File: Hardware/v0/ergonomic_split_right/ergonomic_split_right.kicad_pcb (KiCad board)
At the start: 2 copper layers, 183 x 172.8 mm, 66 parts, among them J2 Left_Interface, SW1 R50, SW10 R31, SW11 R45, SW12 R51, SW13 R02, SW14 R12, SW15 R22, SW16 R32, SW17 R42, SW18 R54, SW19 R03, SW2 R06, SW20 R13, SW21 R23, SW22 R33, SW23 R43, SW24 R53, SW25 R04, SW26 R14, SW27 R24, SW28 R34, SW29 R44, SW3 R16, SW30 R46, SW31 R05, SW32 R15, SW33 R25, SW34 R35, SW35 R55, SW36 R10, SW37 R30, SW39 R00, SW4 R26, SW40 R_Encoder, SW5 R36, SW6 R52, SW7 R01, SW8 R11, SW9 R21, U2 PCAL9555AHF, U9 TCR2EF33

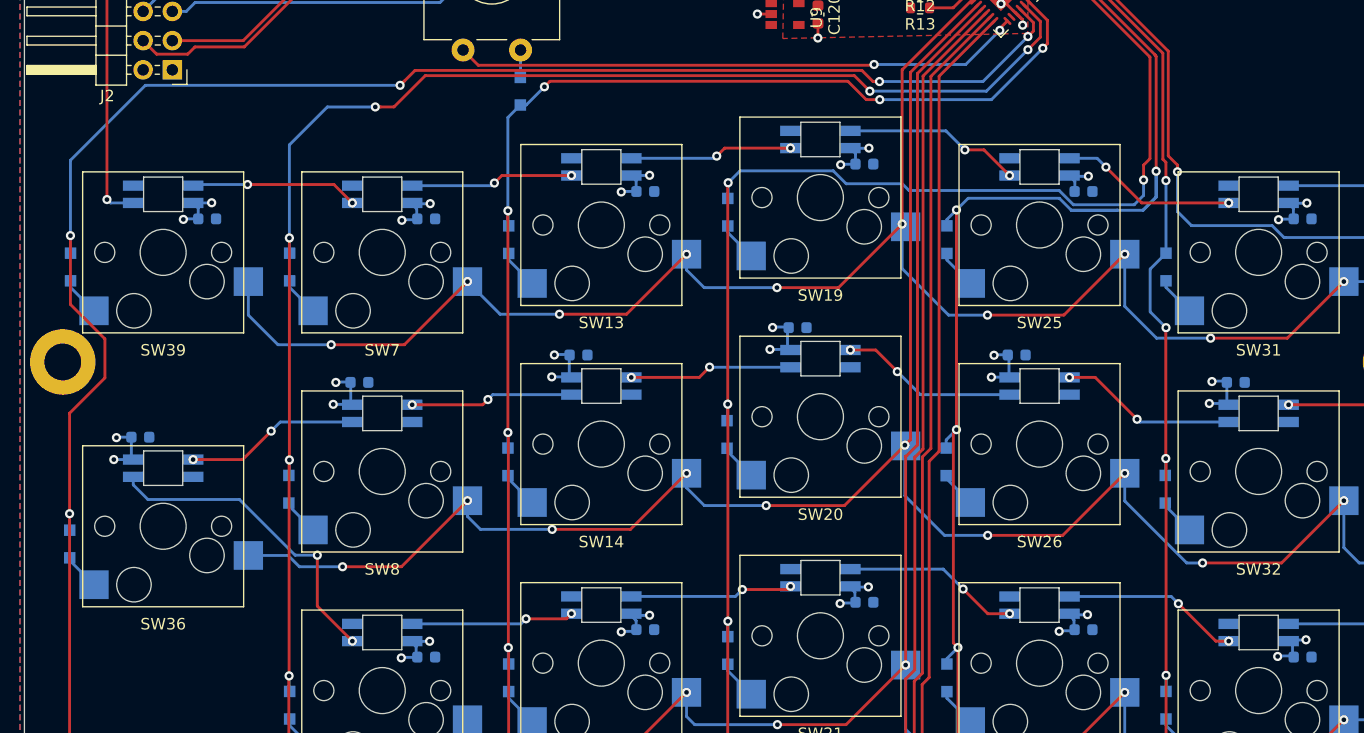
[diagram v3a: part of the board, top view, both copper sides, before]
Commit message: Adding input caps on 5V0
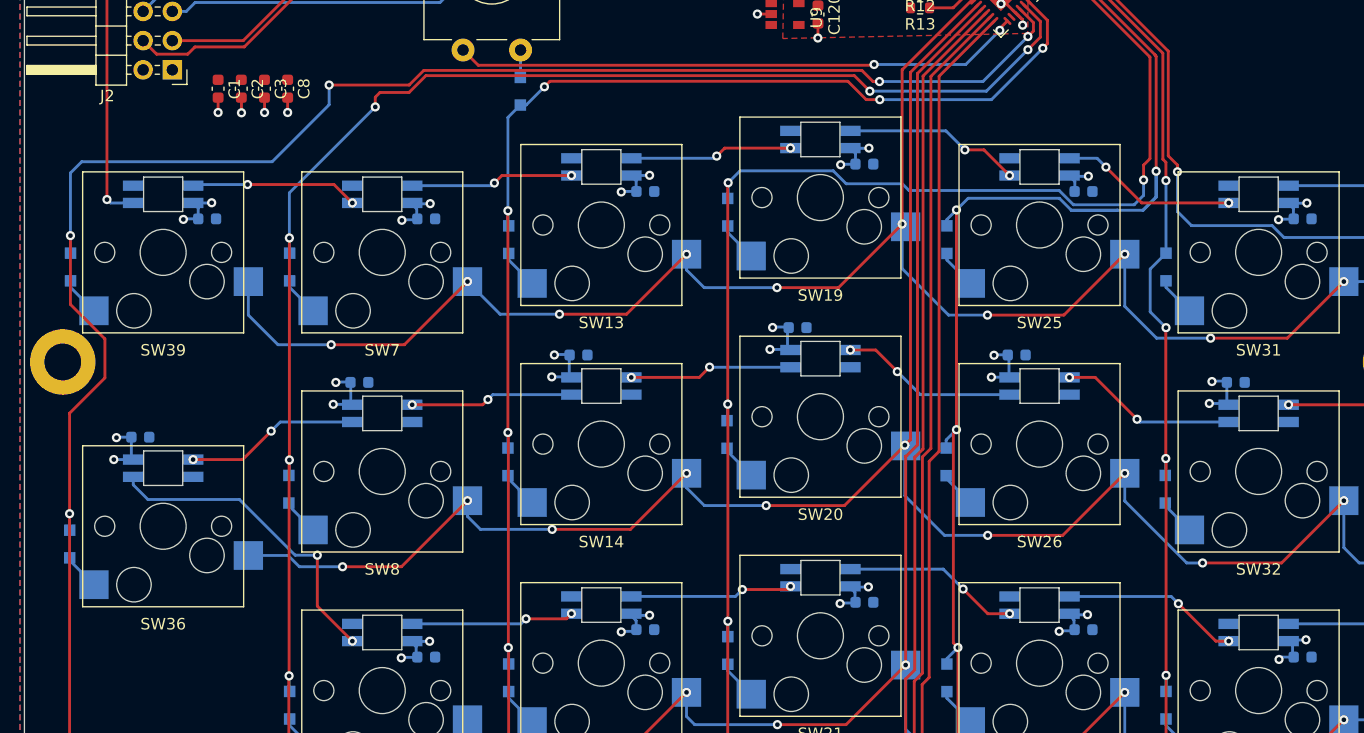
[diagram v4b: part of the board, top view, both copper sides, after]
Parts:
- added C1: 10uF, Capacitor_smd:C_0603_1608Metric, F.Cu at (157.2, 58.8)
- added C2: 1uF, Capacitor_smd:C_0603_1608Metric, F.Cu at (159.2, 58.8)
- added C3: 100nF, Capacitor_smd:C_0603_1608Metric, F.Cu at (161.2, 58.8)
- added C8: 100nF, Capacitor_smd:C_0603_1608Metric, F.Cu at (163.2, 58.8)
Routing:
- net GND: track 22.3 -> 27.4 mm, vias 12 -> 16
- net /IO Expander/COL[1]: track 199.9 -> 197.9 mm

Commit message: Cleaning up silk
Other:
- board text added: "ergonomic split - v0 Alex Binos 2022"
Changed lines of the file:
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@@
   (general
     (thickness 1.6)
-    (drawings 27)
+    (drawings 29)
     (tracks 1280)
     (zones 0)
@@
     (38 B.Mask user)
     (39 F.Mask user)
-    (40 Dwgs.User user)
-    (41 Cmts.User user)
+    (40 Dwgs.User user hide)
+    (41 Cmts.User user hide)
     (42 Eco1.User user)
     (43 Eco2.User user hide)
     (44 Edge.Cuts user)
     (45 Margin user)
-    (46 B.CrtYd user)
-    (47 F.CrtYd user)
-    (48 B.Fab user)
-    (49 F.Fab user)
+    (46 B.CrtYd user hide)
+    (47 F.CrtYd user hide)
+    (48 B.Fab user hide)
+    (49 F.Fab user hide)
   )
   (setup
@@
     (tags capacitor)
     (attr smd)
-    (fp_text reference C8 (at 0 -1.43 90) (layer F.SilkS)
+    (fp_text reference C8 (at -2.54254 -0.1143 90) (layer F.SilkS)
       (effects (font (size 1 1) (thickness 0.15)))
     )
@@
     (tags capacitor)
     (attr smd)
-    (fp_text reference C3 (at 0 -1.43 90) (layer F.SilkS)
+    (fp_text reference C3 (at -2.54254 -0.046568 90) (layer F.SilkS)
       (effects (font (size 1 1) (thickness 0.15)))
     )
@@
     (tags capacitor)
     (attr smd)
-    (fp_text reference C2 (at 0 -1.43 90) (layer F.SilkS)
+    (fp_text reference C2 (at -2.54254 -0.080434 90) (layer F.SilkS)
       (effects (font (size 1 1) (thickness 0.15)))
     )
@@
     (tags capacitor)
     (attr smd)
-    (fp_text reference C1 (at 0 -1.43 90) (layer F.SilkS)
+    (fp_text reference C1 (at -2.54254 -0.0508 90) (layer F.SilkS)
       (effects (font (size 1 1) (thickness 0.15)))
     )
@@
     (tags capacitor)
     (attr smd)
-    (fp_text reference C5 (at 0 -1.43) (layer F.SilkS)
+    (fp_text reference C5 (at -2.60096 0.06096) (layer F.SilkS)
       (effects (font (size 1 1) (thickness 0.15)))
     )
@@
     (tags capacitor)
     (attr smd)
-    (fp_text reference C7 (at 0 -1.43) (layer F.SilkS)
+    (fp_text reference C7 (at 0.06828 1.34112) (layer F.SilkS)
       (effects (font (size 1 1) (thickness 0.15)))
     )
@@
     (tags resistor)
     (attr smd)
-    (fp_text reference R12 (at 0 -1.43) (layer F.SilkS)
+    (fp_text reference R12 (at 2.24536 1.38176) (layer F.SilkS)
       (effects (font (size 1 1) (thickness 0.15)))
     )
@@
     (tags resistor)
     (attr smd)
-    (fp_text reference R13 (at 0 -1.43) (layer F.SilkS)
+    (fp_text reference R13 (at 0.091741 -1.433349) (layer F.SilkS)
       (effects (font (size 1 1) (thickness 0.15)))
     )
@@
     (descr "Alps rotary encoder, EC12E... with switch, vertical shaft, http://www.alps.com/prod/info/E/HTML/Encoder/Incremental/EC11/EC11E15204A3.html")
     (tags "rotary encoder")
-    (fp_text reference SW40 (at 2.8 -4.7 90) (layer F.SilkS)
+    (fp_text reference SW40 (at 3.78206 -5.7023 180) (layer F.SilkS)
       (effects (font (size 1 1) (thickness 0.15)))
     )
@@
     (at 225.237431 50.565538 45)
     (attr smd)
-    (fp_text reference U2 (at 0 -4.2 45) (layer F.SilkS)
+    (fp_text reference U2 (at -2.572775 -3.59901 45) (layer F.SilkS)
       (effects (font (size 1 1) (thickness 0.15)))
     )
@@
   (module custom_footprint_library:TCR2EF33_SOT25 (layer F.Cu)
     (at 205.26756 51.34864 270)
-    (fp_text reference U9 (at 1.24968 -3.937 90) (layer F.SilkS)
+    (fp_text reference U9 (at 3.43916 -1.35636 180) (layer F.SilkS)
       (effects (font (size 1 1) (thickness 0.15)))
     )
@@
       (net 5 +3V3))
   )
+  (gr_text "ergonomic split - v0\nAlex Binos 2022" (at 260.7945 52.2605) (layer F.SilkS)
+    (effects (font (size 1 1) (thickness 0.15)))
+  )
+  (gr_circle (center 222.0976 50.61712) (end 222.176626 50.61712) (layer F.SilkS) (width 0.15))
   (gr_line (start 140.335 129.8194) (end 140.333388 41.022612) (layer Edge.Cuts) (width 0.05))
   (gr_line (start 106.2482 165.2016) (end 139.398629 132.079999) (layer Edge.Cuts) (width 0.05))

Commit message: Tidying last few traces
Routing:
- net /IO Expander/ROW[5]: track 257.9 -> 256.1 mm
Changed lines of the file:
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@@
     (thickness 1.6)
     (drawings 29)
-    (tracks 1280)
+    (tracks 1277)
     (zones 0)
     (modules 70)
@@
       (outputformat 1)
       (mirror false)
-      (drillshape 1)
+      (drillshape 0)
       (scaleselection 1)
-      (outputdirectory ""))
+      (outputdirectory "gerber/"))
   )
   (net 0 "")
@@
   (segment (start 263.3345 71.7296) (end 263.3345 73.18502) (width 0.25) (layer B.Cu) (net 7))
   (via (at 240.5888 66.0146) (size 0.8) (drill 0.4) (layers F.Cu B.Cu) (net 7))
-  (segment (start 240.5888 66.0146) (end 240.5888 65.4304) (width 0.25) (layer F.Cu) (net 7))
-  (segment (start 240.5888 65.4304) (end 239.7887 64.6303) (width 0.25) (layer F.Cu) (net 7))
-  (segment (start 232.070892 47.809132) (end 239.7887 55.52694) (width 0.25) (layer F.Cu) (net 7))
-  (segment (start 227.710984 47.80913) (end 232.070892 47.809132) (width 0.25) (layer F.Cu) (net 7))
-  (segment (start 226.580922 48.939192) (end 227.710984 47.80913) (width 0.25) (layer F.Cu) (net 7))
-  (segment (start 226.510223 48.939192) (end 226.580922 48.939192) (width 0.25) (layer F.Cu) (net 7))
-  (segment (start 239.7887 64.6303) (end 239.7887 55.52694) (width 0.25) (layer F.Cu) (net 7))
   (segment (start 240.5888 66.0146) (end 240.5888 69.47408) (width 0.25) (layer B.Cu) (net 7))
   (segment (start 240.5888 69.47408) (end 241.808 70.69328) (width 0.25) (layer B.Cu) (net 7))
@@
   (segment (start 241.808 70.69328) (end 248.817278 70.69328) (width 0.25) (layer B.Cu) (net 7))
   (segment (start 263.3345 71.7296) (end 249.95886 71.7296) (width 0.25) (layer B.Cu) (net 7))
+  (segment (start 232.070892 47.809132) (end 227.640285 47.80913) (width 0.25) (layer F.Cu) (net 7))
+  (segment (start 239.7887 55.52694) (end 232.070892 47.809132) (width 0.25) (layer F.Cu) (net 7))
+  (segment (start 227.640285 47.80913) (end 226.510223 48.939192) (width 0.25) (layer F.Cu) (net 7))
+  (segment (start 239.7887 64.6303) (end 239.7887 55.52694) (width 0.25) (layer F.Cu) (net 7))
+  (segment (start 240.5888 65.4304) (end 239.7887 64.6303) (width 0.25) (layer F.Cu) (net 7))
+  (segment (start 240.5888 66.0146) (end 240.5888 65.4304) (width 0.25) (layer F.Cu) (net 7))
   (segment (start 153.19375 54.61) (end 159.3596 54.61) (width 0.25) (layer F.Cu) (net 18))
   (segment (start 159.3596 54.61) (end 163.617579 50.352021) (width 0.25) (layer F.Cu) (net 18))
@@
   (segment (start 226.4156 47.619602) (end 225.803116 48.232086) (width 0.25) (layer F.Cu) (net 24))
   (segment (start 226.4156 45.7454) (end 226.4156 47.619602) (width 0.25) (layer F.Cu) (net 24))
-  (segment (start 219.879901 49.321499) (end 219.0364 50.165) (width 0.25) (layer F.Cu) (net 25))
-  (segment (start 222.932732 49.321499) (end 219.879901 49.321499) (width 0.25) (layer F.Cu) (net 25))
-  (segment (start 223.257532 49.646299) (end 222.932732 49.321499) (width 0.25) (layer F.Cu) (net 25))
+  (segment (start 223.257532 49.646299) (end 222.671333 49.0601) (width 0.25) (layer F.Cu) (net 25))
+  (segment (start 220.1413 49.0601) (end 219.0364 50.165) (width 0.25) (layer F.Cu) (net 25))
+  (segment (start 222.671333 49.0601) (end 220.1413 49.0601) (width 0.25) (layer F.Cu) (net 25))
   (segment (start 219.036701 51.759331) (end 221.087469 51.759331) (width 0.25) (layer F.Cu) (net 26))
   (segment (start 222.846947 49.999853) (end 222.903979 49.999853) (width 0.25) (layer F.Cu) (net 26))
@@
   (segment (start 147.79244 183.20004) (end 155.461709 190.869309) (width 0.25) (layer F.Cu) (net 29))
   (via (at 211.4169 153.4541) (size 0.8) (drill 0.4) (layers F.Cu B.Cu) (net 29))
-  (segment (start 218.1225 146.7485) (end 218.1225 146.5961) (width 0.25) (layer F.Cu) (net 29))
-  (segment (start 216.9668 147.9042) (end 218.1225 146.7485) (width 0.25) (layer F.Cu) (net 29))
   (segment (start 211.4169 153.4541) (end 216.9668 147.9042) (width 0.25) (layer F.Cu) (net 29))
   (segment (start 219.8624 57.708336) (end 224.671746 52.89899) (width 0.25) (layer F.Cu) (net 29))
@@
   (segment (start 216.64819 74.43359) (end 216.64819 70.55364) (width 0.25) (layer B.Cu) (net 33))
   (segment (start 211.11613 76.0857) (end 216.64819 70.55364) (width 0.25) (layer F.Cu) (net 33))
-  (segment (start 222.903979 51.131223) (end 222.663979 51.131223) (width 0.25) (layer F.Cu) (net 33))
-  (segment (start 222.663979 51.131223) (end 216.64819 57.147012) (width 0.25) (layer F.Cu) (net 33))
-  (segment (start 216.64819 57.147012) (end 216.64819 70.55364) (width 0.25) (layer F.Cu) (net 33))
   (segment (start 224.0661 78.4733) (end 220.6879 78.4733) (width 0.25) (layer B.Cu) (net 33))
   (segment (start 220.6879 78.4733) (end 216.64819 74.43359) (width 0.25) (layer B.Cu) (net 33))
+  (segment (start 222.896677 51.131223) (end 216.64819 57.37971) (width 0.25) (layer F.Cu) (net 33))
+  (segment (start 222.903979 51.131223) (end 222.896677 51.131223) (width 0.25) (layer F.Cu) (net 33))
+  (segment (start 216.64819 57.37971) (end 216.64819 70.55364) (width 0.25) (layer F.Cu) (net 33))
   (via (at 258.79552 67.8434) (size 0.8) (drill 0.4) (layers F.Cu B.Cu) (net 34))
   (segment (start 258.17343 67.22131) (end 258.79552 67.8434) (width 0.25) (layer B.Cu) (net 34))
@@
   (segment (start 237.6424 65.4304) (end 238.199084 64.873716) (width 0.25) (layer F.Cu) (net 82))
   (segment (start 237.6424 66.7258) (end 237.6424 65.4304) (width 0.25) (layer F.Cu) (net 82))
-  (segment (start 227.570883 49.999853) (end 227.570883 49.939357) (width 0.25) (layer F.Cu) (net 82))
-  (segment (start 227.570883 49.939357) (end 228.35108 49.15916) (width 0.25) (layer F.Cu) (net 82))
   (segment (start 231.318648 49.15916) (end 238.199084 56.039596) (width 0.25) (layer F.Cu) (net 82))
-  (segment (start 228.35108 49.15916) (end 231.318648 49.15916) (width 0.25) (layer F.Cu) (net 82))
   (segment (start 238.199084 64.873716) (end 238.199084 56.039596) (width 0.25) (layer F.Cu) (net 82))
   (via (at 200.41616 156.30398) (size 0.8) (drill 0.4) (layers F.Cu B.Cu) (net 82))
@@
   (segment (start 210.658521 65.930119) (end 202.560581 65.930119) (width 0.25) (layer B.Cu) (net 82))
   (segment (start 237.6424 66.7258) (end 237.6424 68.06692) (width 0.25) (layer B.Cu) (net 82))
+  (segment (start 228.411576 49.15916) (end 227.570883 49.999853) (width 0.25) (layer F.Cu) (net 82))
+  (segment (start 229.30104 49.15916) (end 228.411576 49.15916) (width 0.25) (layer F.Cu) (net 82))
+  (segment (start 229.30104 49.15916) (end 231.318648 49.15916) (width 0.25) (layer F.Cu) (net 82))
   (segment (start 201.48938 71.29698) (end 203.52752 73.33512) (width 0.25) (layer B.Cu) (net 83))
   (segment (start 201.48938 70.72739) (end 201.48938 71.29698) (width 0.25) (layer B.Cu) (net 83))
